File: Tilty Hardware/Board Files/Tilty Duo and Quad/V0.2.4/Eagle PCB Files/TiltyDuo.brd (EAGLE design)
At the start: 38.1 x 50.8 mm, 47 parts, among them U1 TEENSY_3.0_OUTER-PINS28-DIP_S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, U2 HC-09_BREAKOUT, U3 MPL3115A2LGA8, U4 LM2931, U5 MPU-6050, U6 HMC5883LSMD, U7 SPI_FLASH-X25XXSMD

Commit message: Added lots of stuff!
Added a completed Advanced IMU add-on prototype
Added a Spektrum Satellite R/C receiver library
Added Spektrum Satellite R/C receiver testing code
Added a Tilty PCB template
Fixed a bug in the PID library
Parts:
- C5: value 0.1uF -> 4.7uF
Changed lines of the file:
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@@
 </element>
 <element name="C4" library="resistor" package="C0603" value="0.1uF" x="22.987" y="40.259" smashed="yes" rot="MR90"/>
-<element name="C5" library="resistor" package="C0603" value="0.1uF" x="15.113" y="40.259" smashed="yes" rot="MR90"/>
+<element name="C5" library="resistor" package="C0603" value="4.7uF" x="15.113" y="40.259" smashed="yes" rot="MR90"/>
 <element name="U1" library="My Parts" package="28-DIP" value="TEENSY_3.0_OUTER-PINS28-DIP_SOCKET" x="19.05" y="32.893">
 <attribute name="COST" value="0.28" x="19.05" y="32.893" size="1.778" layer="27" display="off"/>

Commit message: Tilty PCB work
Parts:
- added D6: (no value), diode:DO214AA
- added SJ6: SOLDERJUMPERTRACE, SparkFun-Passives:SJ_2S-TRACE
- JP1, JP2: value (none) -> 8-PIN_HEADER; device pinhead:1X08_NO_SS_LOCKING -> My Parts:8-PIN_RECEPTACLE_LOCK_NO-SS
- JP3: value (none) -> 8-PIN_HEADER; device pinhead:2X03_NO_SS_LOCK -> My Parts:8-PIN_RECEPTACLE_LOCK_NO-SS
- JP4: value 2-POS_SMD_TERM_BLOCK -> 8-PIN_HEADER; device My Parts:2-POS_SMD_TERMINAL_BLOCK -> My Parts:8-PIN_RECEPTACLE_LOCK_NO-SS
- JP5: value (none) -> 2-POS_SMD_TERM_BLOCK; device pinhead:1X08_NO_SS_LOCKING -> My Parts:2-POS_SMD_TERMINAL_BLOCK
- JP6: device pinhead:1X08_NO_SS_LOCKING -> pinhead:2X03_NO_SS_LOCK
- SJ2: device SparkFun-Passives:SJ_3 -> SparkFun-Passives:SJ_3_PASTE1&2
- moved JP3 38.0 mm to (35.6, 20.2), turned to 270 degrees
- moved JP6 38.0 mm to (2.67, 39.2)
- moved JP4 36.3 mm to (30.5, 40.5), turned to 270 degrees
- moved JP5 36.3 mm to (19.1, 6.10), turned to 0 degrees
- moved SJ4 4.58 mm to (18.3, 13.7)
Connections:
- net 5V: now also JP4.P$1; no longer JP5.8
- net AUXCL: now also JP3.P$7; no longer JP6.2
- net AUXDA: now also JP3.P$6; no longer JP6.3
- net BATT_SENSE: now also JP3.P$4; no longer JP6.5
- net BT_CMD: now also JP3.P$3; no longer JP6.6
- net CS: now also JP1.P$1; no longer JP1.1
- net GND: now also JP2.P$1, JP3.P$8, JP4.P$2, JP5.P$4, JP6.2; no longer JP2.1, JP3.1, JP3.2, JP4.P$4, JP5.7
- net I/O1: now also JP1.P$5, JP6.6; no longer JP1.5, JP3.6
- net I/O2: now also JP1.P$4, JP6.5; no longer JP1.4, JP3.5
- net I/O3: now also JP4.P$3; no longer JP5.6
- net I/O4: now also JP4.P$4; no longer JP5.5
- net MISO: now also JP2.P$3; no longer JP2.3
- net MOSI: now also JP2.P$4; no longer JP2.4
- net MPU_INT: now also JP1.P$2; no longer JP1.2
- net N$10: now also JP3.P$1; no longer JP6.8
- net N$12: now also JP2.P$6; no longer JP2.6
- net N$18: now also JP4.P$5; no longer JP5.4
- net N$19: now also JP4.P$6; no longer JP5.3
- net N$23: now also JP3.P$2; no longer JP6.7
- net N$7: now also JP1.P$3; no longer JP1.3
- net N$8: now also JP2.P$5; no longer JP2.5
- net POW_I/O1: now also JP6.3, JP6.4; no longer JP3.3, JP3.4
- net RX1: now also JP1.P$7; no longer JP1.7
- net RX3: now also JP2.P$8; no longer JP2.8
- net SCK: now also JP3.P$5; no longer JP6.4
- net SCL: now also JP4.P$7; no longer JP5.2
- net SDA: now also JP4.P$8; no longer JP5.1
- net TEENSY_3V3: now also JP1.P$8; no longer JP1.8
- net TX1: now also JP1.P$6; no longer JP1.6
- net TX3: now also JP2.P$7; no longer JP2.7
- net VBATT: now also D6.A, D6.C, JP2.P$2, JP5.P$3, SJ6.1, SJ6.2; no longer JP2.2, JP4.P$3
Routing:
- net VBATT: track 73.1 -> 67.4 mm
- net N$9: track 6.00 -> 2.84 mm
- net TEENSY_3V3: track 151.4 -> 152.6 mm
- net GND: track 56.1 -> 56.7 mm
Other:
- board text added: "Sep 2013"
- board text removed: "Aug 2013"

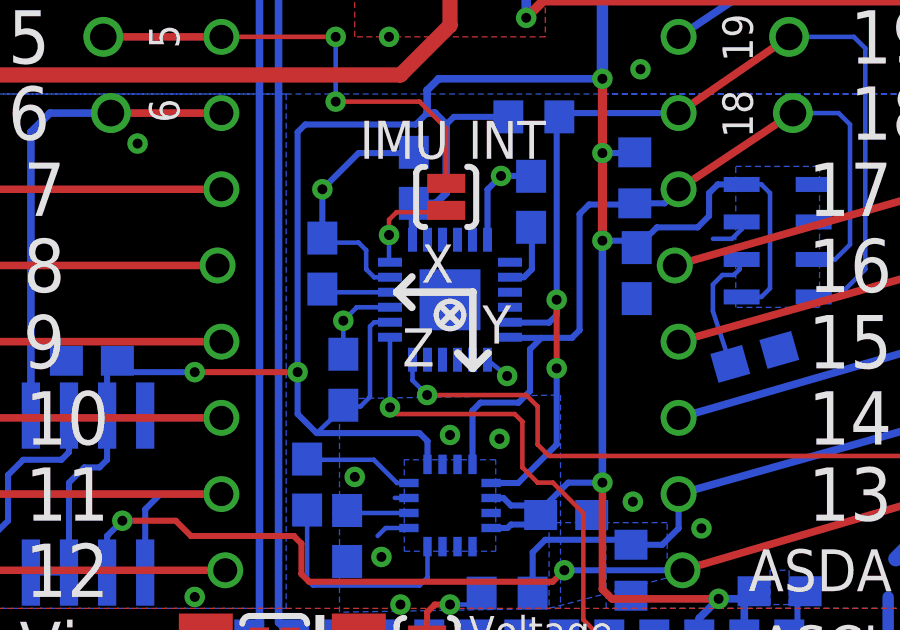
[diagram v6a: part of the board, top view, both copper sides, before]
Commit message: Finished Tilty Duo/Quad 0.2.4, work on motor driver
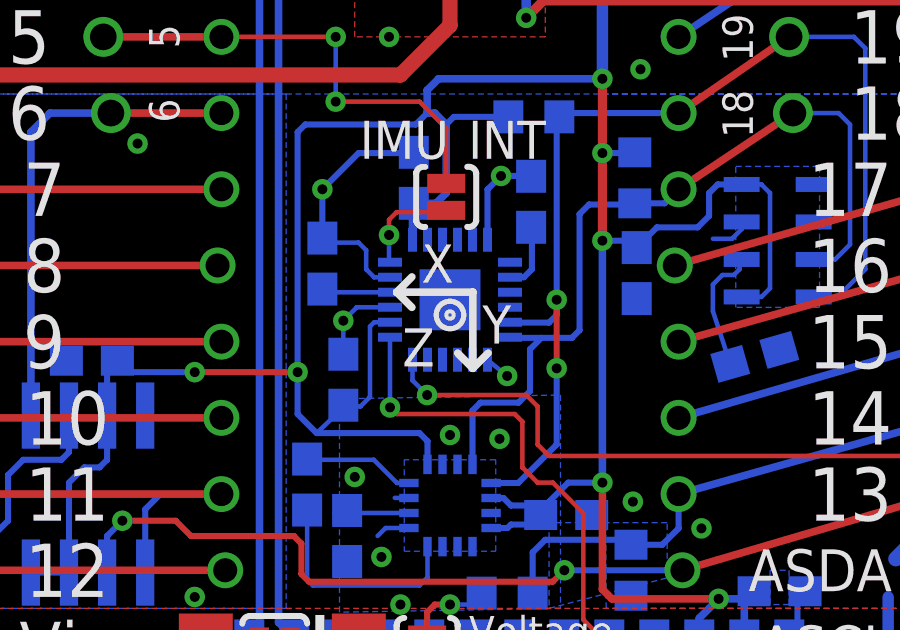
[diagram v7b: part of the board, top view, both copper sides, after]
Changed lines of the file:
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@@
 <setting verticaltext="up"/>
 </settings>
-<grid distance="0.01" unitdist="inch" unit="inch" style="lines" multiple="1" display="yes" altdistance="0.005" altunitdist="inch" altunit="inch"/>
+<grid distance="0.01" unitdist="inch" unit="inch" style="lines" multiple="1" display="yes" altdistance="0.0025" altunitdist="inch" altunit="inch"/>
 <layers>
 <layer number="1" name="Top" color="4" fill="1" visible="yes" active="yes"/>
@@
 <wire x1="17.272" y1="25.654" x2="17.78" y2="26.162" width="0.254" layer="25"/>
 <circle x="19.05" y="24.892" radius="0.457903125" width="0.1778" layer="25"/>
-<wire x1="19.05" y1="24.892" x2="18.7325" y2="25.2095" width="0.2032" layer="25"/>
-<wire x1="19.3675" y1="25.2095" x2="19.05" y2="24.892" width="0.2032" layer="25"/>
-<wire x1="19.05" y1="24.892" x2="19.3675" y2="24.5745" width="0.2032" layer="25"/>
-<wire x1="18.7325" y1="24.5745" x2="19.05" y2="24.892" width="0.2032" layer="25"/>
 <text x="18.0975" y="25.9715" size="1.27" layer="25" ratio="15">X</text>
 <text x="20.1295" y="23.9395" size="1.27" layer="25" ratio="15">Y</text>
@@
 <text x="18.923" y="35.941" size="1.27" layer="26" ratio="15" rot="MR0" align="center">5v</text>
 <text x="9.525" y="47.879" size="1.016" layer="26" ratio="12" rot="MR90" align="center-left">3v3</text>
+<circle x="19.05" y="24.892" radius="0.0635" width="0.254" layer="25"/>
 </plain>
 <attributes>
@@
 <attribute name="VALUE" x="14.986" y="48.5775" size="0.4064" layer="28" rot="MR0"/>
 <attribute name="PART#" value="BZX84C3V3LT1GOSCT-ND" x="13.97" y="48.768" size="1.778" layer="28" rot="MR0" display="off"/>
+<attribute name="PART#2" value="MMBZ5226B-FDICT-ND" x="13.97" y="48.768" size="1.778" layer="28" rot="MR0" display="off"/>
 </element>
 <element name="JP4" library="My Parts" package="8-PIN_RECEPTACLE_LOCK_NO-SS" value="8-PIN_HEADER" x="30.48" y="40.513" rot="R270"/>

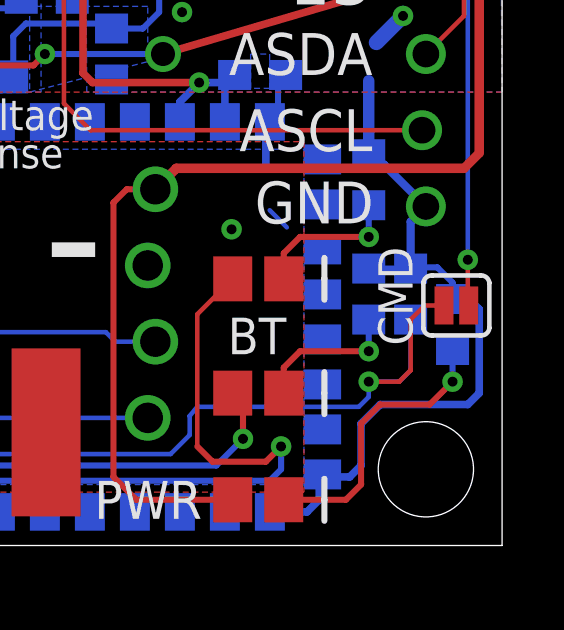
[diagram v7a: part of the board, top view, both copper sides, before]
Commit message: Updated bluetooth command jumper to a cuttable trace solder jumper
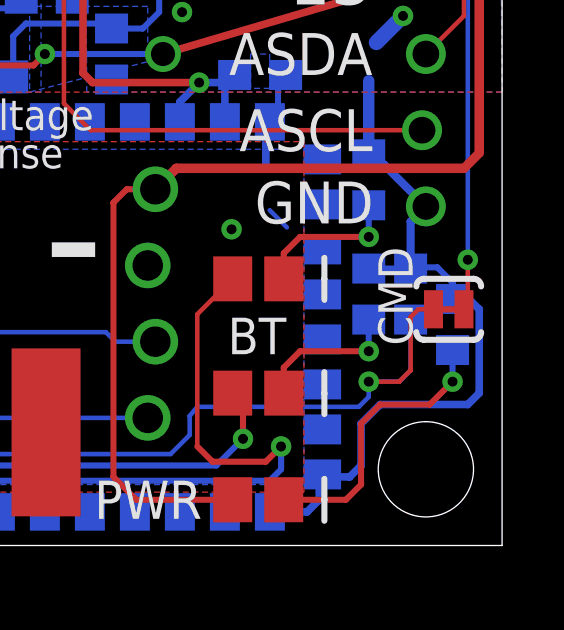
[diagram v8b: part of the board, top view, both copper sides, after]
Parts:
- SJ5: value (none) -> SOLDERJUMPERTRACE; device SparkFun-Passives:SJ_2S -> SparkFun-Passives:SJ_2S-TRACE
- moved SJ5 0.28 mm to (36.3, 7.87)
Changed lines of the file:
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@@
 <attribute name="VALUE" x="19.939" y="12.7635" size="0.4064" layer="27" rot="R90"/>
-</element>
-<element name="SJ5" library="SparkFun-Passives" package="SJ_2S" value="" x="36.576" y="8.001" smashed="yes" rot="R180">
-<attribute name="VALUE" x="37.5258" y="9.652" size="0.4064" layer="27" rot="R180"/>
 </element>
 <element name="D4" library="SparkFun-DiscreteSemi" package="SOT23-3" value="" x="24.13" y="48.768" smashed="yes" rot="MR0">
@@
 <element name="D6" library="diode" package="DO214AA" value="" x="13.462" y="13.843" smashed="yes" rot="R180">
 <attribute name="VALUE" x="16.102" y="16.549" size="1.27" layer="27" ratio="10" rot="R180"/>
+</element>
+<element name="SJ5" library="SparkFun-Passives" package="SJ_2S-TRACE" value="SOLDERJUMPERTRACE" x="36.322" y="7.874" smashed="yes" rot="R180">
+<attribute name="VALUE" x="37.2745" y="9.525" size="0.4064" layer="27" rot="R180"/>
 </element>
 </elements>
@@
 <wire x1="12.3825" y1="1.8415" x2="13.589" y2="3.048" width="0.1524" layer="16"/>
 <wire x1="27.051" y1="3.048" x2="27.686" y2="3.683" width="0.1524" layer="16"/>
-<contactref element="SJ5" pad="2"/>
 <via x="33.655" y="5.461" extent="1-16" drill="0.3302"/>
 <wire x1="33.3248" y1="4.6228" x2="27.94" y2="4.6228" width="0.1524" layer="16"/>
@@
 <wire x1="35.052" y1="5.842" x2="34.671" y2="5.461" width="0.1524" layer="1"/>
 <wire x1="34.671" y1="5.461" x2="33.655" y2="5.461" width="0.1524" layer="1"/>
-<wire x1="36.1641" y1="8.001" x2="35.521" y2="8.001" width="0.1524" layer="1"/>
-<wire x1="35.521" y1="8.001" x2="35.052" y2="7.532" width="0.1524" layer="1"/>
-<wire x1="35.052" y1="7.532" x2="35.052" y2="5.842" width="0.1524" layer="1"/>
+<wire x1="35.052" y1="7.62" x2="35.052" y2="5.842" width="0.1524" layer="1"/>
+<contactref element="SJ5" pad="2"/>
+<wire x1="35.052" y1="7.62" x2="35.306" y2="7.874" width="0.1524" layer="1"/>
+<wire x1="35.306" y1="7.874" x2="35.814" y2="7.874" width="0.1524" layer="1"/>
 </signal>
 <signal name="TEENSY_3V3" class="3">
@@
 <signal name="BT_CMD">
 <contactref element="U1" pad="P$26"/>
-<contactref element="SJ5" pad="1"/>
 <wire x1="35.814" y1="24.003" x2="36.957" y2="22.86" width="0.1524" layer="16"/>
 <via x="36.957" y="9.525" extent="1-16" drill="0.3302"/>
 <wire x1="36.957" y1="22.86" x2="36.957" y2="9.525" width="0.1524" layer="16"/>
-<wire x1="36.957" y1="9.525" x2="36.957" y2="8.0319" width="0.1524" layer="1"/>
-<wire x1="36.957" y1="8.0319" x2="36.9879" y2="8.001" width="0.1524" layer="1"/>
 <contactref element="JP3" pad="P$3"/>
 <wire x1="26.67" y1="21.463" x2="35.433" y2="24.003" width="0.254" layer="16"/>
 <wire x1="35.433" y1="24.003" x2="35.814" y2="24.003" width="0.1524" layer="16"/>
+<contactref element="SJ5" pad="1"/>
+<wire x1="36.957" y1="9.525" x2="36.957" y2="8.001" width="0.1524" layer="1"/>
+<wire x1="36.957" y1="8.001" x2="36.83" y2="7.874" width="0.1524" layer="1"/>
 </signal>
 <signal name="N$20">
